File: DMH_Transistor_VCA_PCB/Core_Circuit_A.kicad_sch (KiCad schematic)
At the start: 28 parts, among them Q1 BC548, Q2 BC548, U1 TL074

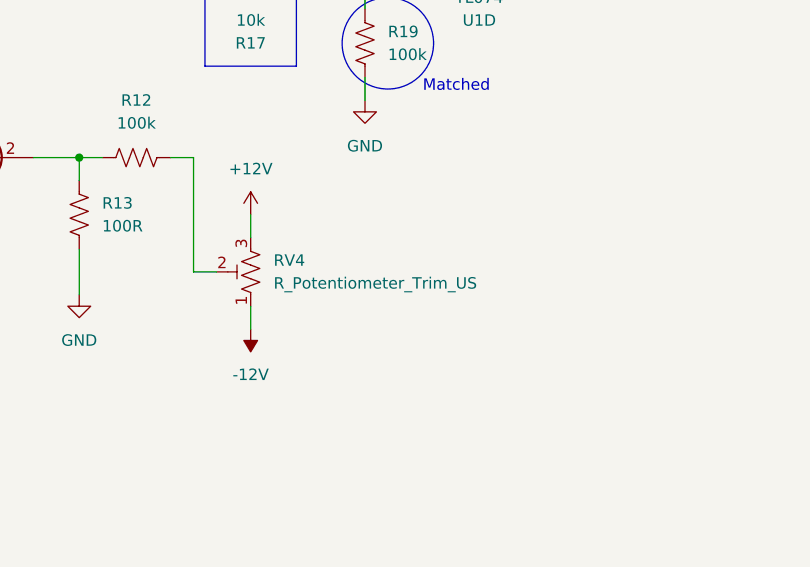
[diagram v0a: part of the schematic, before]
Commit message: Finished core circuit schematic
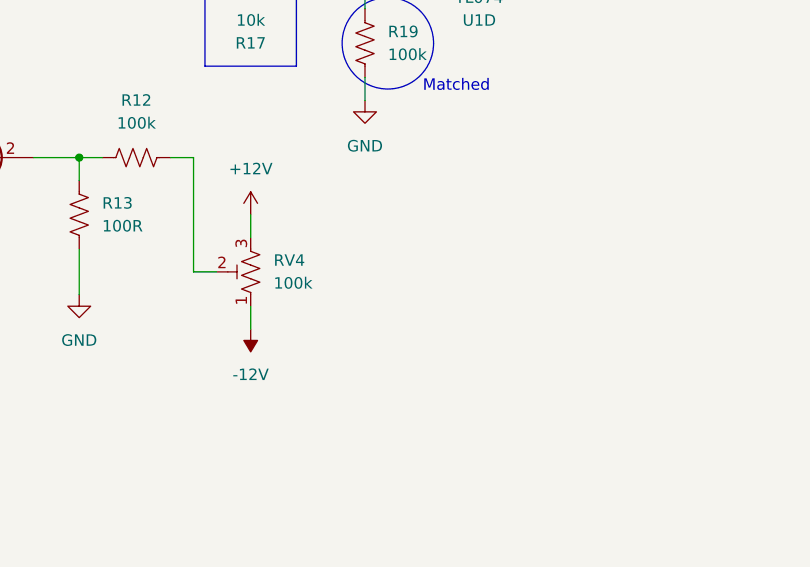
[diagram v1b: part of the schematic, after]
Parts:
- RV4: value R_Potentiometer_Trim_US -> 100k

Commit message: Finished schematic
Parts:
- removed RV1, RV2: 100k, SynthStuff:Potentiometer_TT_P110KH1, symbol Device:R_Potentiometer_US
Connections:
- net CV 1 A Pot: now reaches U1.3 (+)
- net CV 2 A Pot: now reaches U1.5 (+)
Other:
- moved on the sheet: Q1, Q2, R1, R10, R11, R12, R13, R14, R15, R2, R21, R3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

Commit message: Finished main PCB
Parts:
- removed R21: 20k, Resistor_THT:R_Axial_DIN0207_L6.3mm_D2.5mm_P7.62mm_Horizontal, symbol Device:R_US
- removed RV3: 100k, SynthStuff:Potentiometer_Alpha_RD901F-40-00D_Single_Vertical, symbol Device:R_Potentiometer_US
- Q2: footprint Package_TO_SOT_THT:TO-92_Inline -> Package_TO_SOT_THT:TO-92L_Inline_Wide
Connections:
- net Offset A Pot: now reaches R7.1

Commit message: Pots PCB in progress
Need to add CV input traces to the pin headers
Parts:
- renumbered RV4 to RV7
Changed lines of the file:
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@@
 		(dnp no)
 		(fields_autoplaced yes)
-		(property "Reference" "RV4"
+		(property "Reference" "RV7"
 			(at 224.79 100.3299 0)
 			(effects
@@
 			(project "DMH_Transistor_VCA_PCB"
 				(path "/58f4306d-5387-4983-bb08-41a2313fd315/7ad2d702-dfb7-4d49-a82d-34430dd5948f"
-					(reference "RV4")
+					(reference "RV7")
 					(unit 1)
 				)

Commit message: Added CV input attenuverter adjustment trimpots
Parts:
- removed R2, R5: 100k, Resistor_THT:R_Axial_DIN0207_L6.3mm_D2.5mm_P7.62mm_Horizontal, symbol Device:R_US
- added RV10, RV9: 50k, Potentiometer_THT:Potentiometer_Bourns_3296W_Vertical, symbol Device:R_Potentiometer_Trim_US
- R1, R4: value 100k -> 33k
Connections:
- net CV 1 A Input: now also RV9.1
- net CV 2 A Input: now also RV10.1
- net at R1.1, U1.2 (-): now also RV9.2, RV9.3
- net at R4.1, U1.6 (-): now also RV10.2, RV10.3

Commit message: Switched attenuverters trimpot and Rf positions
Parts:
- RV10: Function Center zero adjust -> Zero adj 2A
- RV9: Function Center zero adjust -> Zero adj 1A
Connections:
- net CV 1 A Input: now also R1.1; no longer RV9.1
- net CV 2 A Input: now also R4.1; no longer RV10.1
- net at R6.1, U1.7: now also RV10.2, RV10.3; no longer R4.2
- net at R3.1, U1.1: now also RV9.2, RV9.3; no longer R1.2
- new net: R4.2, RV10.1, U1.6 (-)
- new net: R1.2, RV9.1, U1.2 (-)
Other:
- moved on the sheet: R1, R4, RV10, RV9

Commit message: Changed R8 and R41 to 100k
... in order to remove gain reduction of the incoming CV and offset
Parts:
- R8: value 82k -> 100k
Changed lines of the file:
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@@
 			)
 		)
-		(property "Value" "82k"
+		(property "Value" "100k"
 			(at 138.43 110.49 90)
 			(effects
